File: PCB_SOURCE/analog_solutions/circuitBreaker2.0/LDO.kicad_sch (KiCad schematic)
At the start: 4 parts, among them U201 L78L05_SOT89

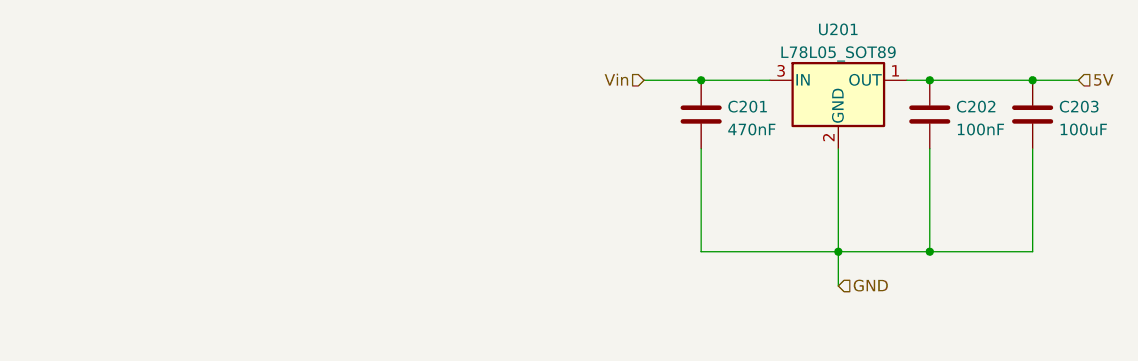
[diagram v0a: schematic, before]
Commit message: fixed bug in ahob program among others
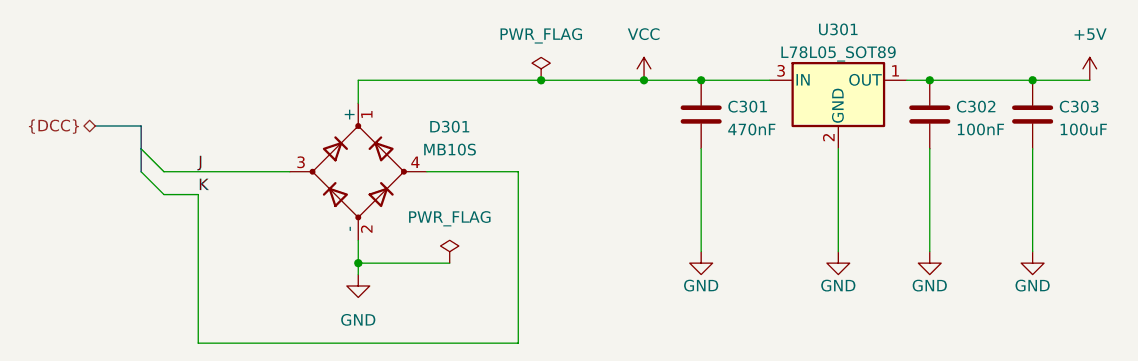
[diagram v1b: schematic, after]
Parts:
- added D301: MB10S, Package_TO_SOT_SMD:TO-269AA, symbol custom_kicad_lib_sk:MB10S
- renumbered C201 to C301, C202 to C302, C203 to C303, U201 to U301
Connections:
- net GND: now also D301.2 (-)
- net 5V renamed +5V
- net Vin renamed VCC
- net VCC: now also D301.1 (+)
- new net J: D301.3
- new net K: D301.4
